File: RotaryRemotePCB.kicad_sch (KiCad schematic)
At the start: 10 parts, among them J3 i2c, J4 Neopixel Connector, J5 EncoderRotary, J6 EncoderSwitch, SW1 RotaryEncoder_Switch, U1 TP4056, U2 WeMos_D1_mini, U3 magnetic-charger, U4 TTL

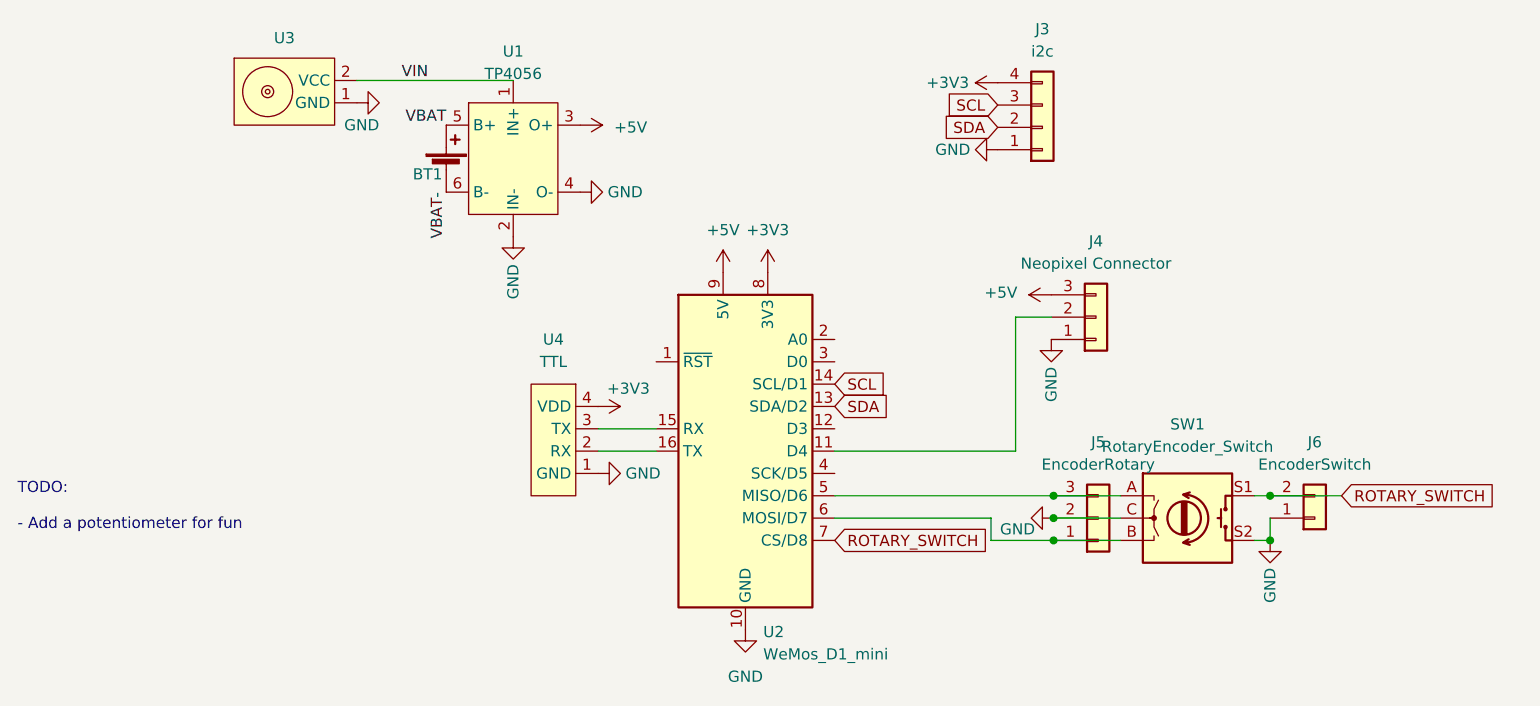
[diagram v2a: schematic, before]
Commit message: Update I2C Bus
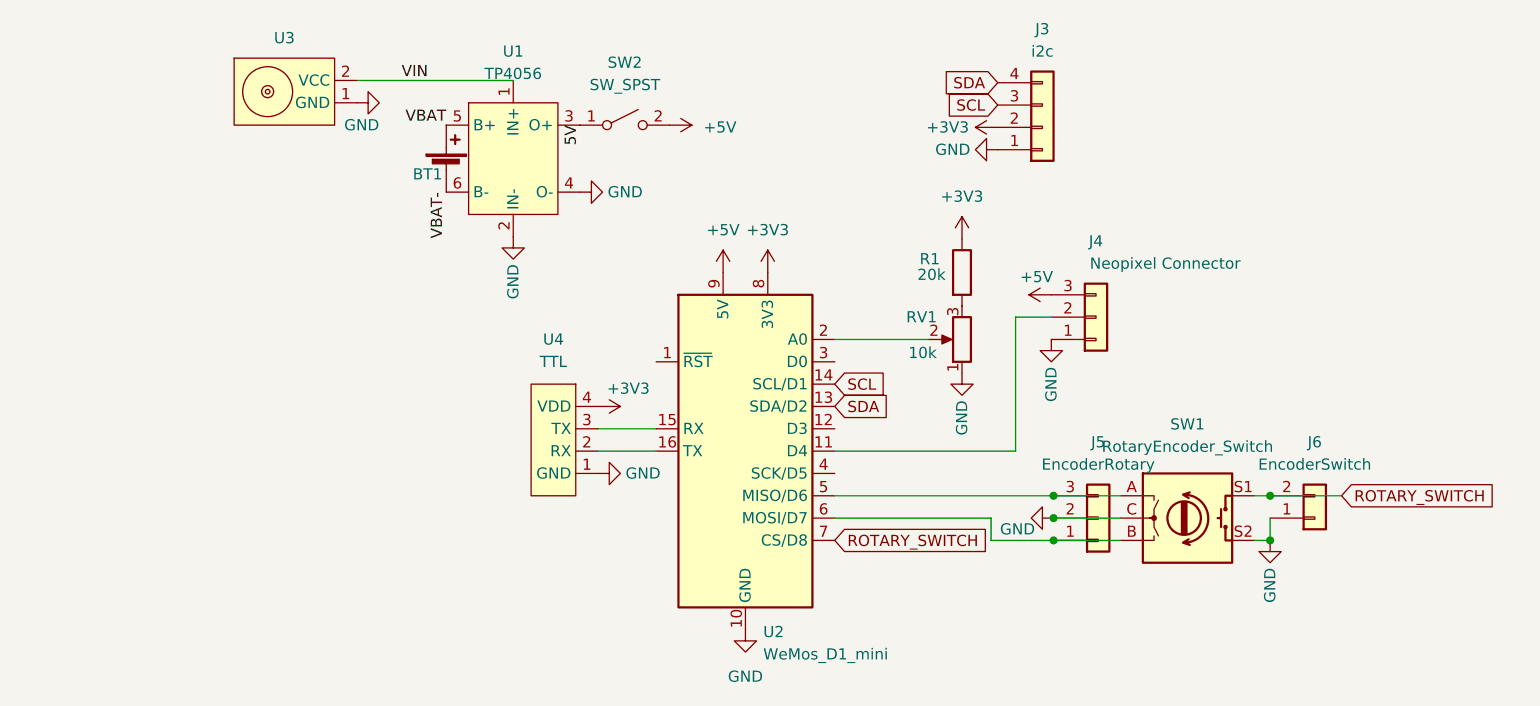
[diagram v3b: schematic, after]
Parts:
- added R1: 20k, Resistor_THT:R_Axial_DIN0207_L6.3mm_D2.5mm_P7.62mm_Horizontal, symbol Device:R
- added RV1: 10k, Potentiometer_THT:Potentiometer_Piher_PT-6-V_Vertical, symbol Device:R_Potentiometer
- added SW2: SW_SPST, Button_Switch_SMD:SW_SPDT_CK-JS102011SAQN, symbol Switch:SW_SPST
- SW1: footprint Rotary_Encoder:RotaryEncoder_Alps_EC12E-Switch_Vertical_H20mm -> (none)
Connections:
- net +3V3: now also J3.2 (Pin_2), R1.1; no longer J3.4 (Pin_4)
- net +5V: now also SW2.2 (B); no longer U1.3 (O+)
- net GND: now also RV1.1
- net SDA: now also J3.4 (Pin_4); no longer J3.2 (Pin_2)
- net at U2.2 (A0): now also RV1.2
- new net: R1.2, RV1.3
- new net 5V: SW2.1 (A), U1.3 (O+)
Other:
- note removed: "TODO: - Add a potentiometer for fun"
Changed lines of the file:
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@@
+    (stroke (width 0) (type default) (color 0 0 0 0))
+  )
+  (wire (pts (xy 181.102 68.326) (xy 191.77 68.326))
     (stroke (width 0) (type default) (color 0 0 0 0))
   )
@@
     (stroke (width 0) (type default) (color 0 0 0 0))
   )
-  (text "TODO:\n\n- Add a potentiometer for fun" (at 88.138 90.17 0)
-    (effects (font (size 1.27 1.27)) (justify left bottom))
-  )
   (label "VBAT-" (at 136.906 51.562 270)
+    (effects (font (size 1.27 1.27)) (justify right bottom))
+  )
+  (label "5V" (at 152.146 43.942 270)
     (effects (font (size 1.27 1.27)) (justify right bottom))
   )
@@
     )
   )
-  (global_label "SDA" (shape input) (at 199.644 44.196 180) (fields_autoplaced)
+  (global_label "SDA" (shape input) (at 199.644 39.116 180) (fields_autoplaced)
     (effects (font (size 1.27 1.27)) (justify right))
-    (property "Intersheet References" "${INTERSHEET_REFS}" (id 0) (at 193.6628 44.1166 0)
+    (property "Intersheet References" "${INTERSHEET_REFS}" (id 0) (at 193.6628 39.0366 0)
       (effects (font (size 1.27 1.27)) (justify right) hide)
     )
@@
       (effects (font (size 1.27 1.27)) hide)
     )
-    (property "Value" "+5V" (id 1) (at 198.12 62.992 90)
+    (property "Value" "+5V" (id 1) (at 202.184 61.214 90)
       (effects (font (size 1.27 1.27)) (justify right))
     )
@@
     (pin "4")
   )
-  (symbol (lib_id "power:+5V") (at 152.146 43.942 270) (unit 1)
-    (in_bom yes) (on_board yes)
-    (property "Reference" "#PWR0106" (id 0) (at 148.336 43.942 0)
-      (effects (font (size 1.27 1.27)) hide)
-    )
-    (property "Value" "+5V" (id 1) (at 159.766 44.196 90)
+  (symbol (lib_id "power:+5V") (at 162.306 43.942 270) (unit 1)
+    (in_bom yes) (on_board yes)
+    (property "Reference" "#PWR0106" (id 0) (at 158.496 43.942 0)
+      (effects (font (size 1.27 1.27)) hide)
+    )
+    (property "Value" "+5V" (id 1) (at 169.926 44.196 90)
       (effects (font (size 1.27 1.27)) (justify right))
     )
-    (property "Footprint" "" (id 2) (at 152.146 43.942 0)
-      (effects (font (size 1.27 1.27)) hide)
-    )
-    (property "Datasheet" "" (id 3) (at 152.146 43.942 0)
+    (property "Footprint" "" (id 2) (at 162.306 43.942 0)
+      (effects (font (size 1.27 1.27)) hide)
+    )
+    (property "Datasheet" "" (id 3) (at 162.306 43.942 0)
       (effects (font (size 1.27 1.27)) hide)
     )
@@
     (pin "4")
   )
+  (symbol (lib_id "Device:R_Potentiometer") (at 195.58 68.326 180) (unit 1)
+    (in_bom yes) (on_board yes)
+    (property "Reference" "RV1" (id 0) (at 189.23 65.786 0)
+      (effects (font (size 1.27 1.27)) (justify right))
+    )
+    (property "Value" "10k" (id 1) (at 189.484 69.85 0)
+      (effects (font (size 1.27 1.27)) (justify right))
+    )
+    (property "Footprint" "Potentiometer_THT:Potentiometer_Piher_PT-6-V_Vertical" (id 2) (at 195.58 68.326 0)
+      (effects (font (size 1.27 1.27)) hide)
+    )
+    (property "Datasheet" "~" (id 3) (at 195.58 68.326 0)
+      (effects (font (size 1.27 1.27)) hide)
+    )
+    (pin "1")
+    (pin "2")
+    (pin "3")
+  )
   (symbol (lib_id "magnetic-charger:magnetic-charger") (at 119.126 40.132 0) (unit 1)
     (in_bom yes) (on_board yes) (fields_autoplaced)
@@
     (pin "1")
   )
+  (symbol (lib_id "Switch:SW_SPST") (at 157.226 43.942 0) (unit 1)
+    (in_bom yes) (on_board yes) (fields_autoplaced)
+    (property "Reference" "SW2" (id 0) (at 157.226 36.83 0))
+    (property "Value" "SW_SPST" (id 1) (at 157.226 39.37 0))
+    (property "Footprint" "Button_Switch_SMD:SW_SPDT_CK-JS102011SAQN" (id 2) (at 157.226 43.942 0)
+      (effects (font (size 1.27 1.27)) hide)
+    )
+    (property "Datasheet" "~" (id 3) (at 157.226 43.942 0)
+      (effects (font (size 1.27 1.27)) hide)
+    )
+    (pin "1")
+    (pin "2")
+  )
+  (symbol (lib_id "power:+3V3") (at 195.58 56.896 0) (unit 1)
+    (in_bom yes) (on_board yes) (fields_autoplaced)
+    (property "Reference" "#PWR0117" (id 0) (at 195.58 60.706 0)
+      (effects (font (size 1.27 1.27)) hide)
+    )
+    (property "Value" "+3V3" (id 1) (at 195.58 52.07 0))
+    (property "Footprint" "" (id 2) (at 195.58 56.896 0)
+      (effects (font (size 1.27 1.27)) hide)
+    )
+    (property "Datasheet" "" (id 3) (at 195.58 56.896 0)
+      (effects (font (size 1.27 1.27)) hide)
+    )
+    (pin "1")
+  )
   (symbol (lib_id "Device:Battery_Cell") (at 136.906 49.022 0) (unit 1)
     (in_bom yes) (on_board yes)
@@
   )
   (symbol (lib_id "Connector_Generic:Conn_01x03") (at 210.82 65.786 0) (mirror x) (unit 1)
-    (in_bom yes) (on_board yes) (fields_autoplaced)
+    (in_bom yes) (on_board yes)
     (property "Reference" "J4" (id 0) (at 210.82 57.15 0))
-    (property "Value" "Neopixel Connector" (id 1) (at 210.82 59.69 0))
+    (property "Value" "Neopixel Connector" (id 1) (at 218.694 59.69 0))
     (property "Footprint" "Connector_PinHeader_2.54mm:PinHeader_1x03_P2.54mm_Horizontal" (id 2) (at 210.82 65.786 0)
       (effects (font (size 1.27 1.27)) hide)
@@
     (pin "2")
     (pin "3")
+  )
+  (symbol (lib_id "Device:R") (at 195.58 60.706 0) (unit 1)
+    (in_bom yes) (on_board yes)
+    (property "Reference" "R1" (id 0) (at 190.754 59.182 0)
+      (effects (font (size 1.27 1.27)) (justify left))
+    )
+    (property "Value" "20k" (id 1) (at 190.5 60.96 0)
+      (effects (font (size 1.27 1.27)) (justify left))
+    )
+    (property "Footprint" "Resistor_THT:R_Axial_DIN0207_L6.3mm_D2.5mm_P7.62mm_Horizontal" (id 2) (at 193.802 60.706 90)
+      (effects (font (size 1.27 1.27)) hide)
+    )
+    (property "Datasheet" "~" (id 3) (at 195.58 60.706 0)
+      (effects (font (size 1.27 1.27)) hide)
+    )
+    (pin "1")
+    (pin "2")
   )
   (symbol (lib_id "Connector_Generic:Conn_01x02") (at 235.712 88.646 0) (mirror x) (unit 1)
@@
     (pin "9")
   )
-  (symbol (lib_id "power:+3V3") (at 199.644 39.116 90) (unit 1)
-    (in_bom yes) (on_board yes)
-    (property "Reference" "#PWR0114" (id 0) (at 203.454 39.116 0)
-      (effects (font (size 1.27 1.27)) hide)
-    )
-    (property "Value" "+3V3" (id 1) (at 191.516 39.116 90)
+  (symbol (lib_id "power:+3V3") (at 199.644 44.196 90) (unit 1)
+    (in_bom yes) (on_board yes)
+    (property "Reference" "#PWR0114" (id 0) (at 203.454 44.196 0)
+      (effects (font (size 1.27 1.27)) hide)
+    )
+    (property "Value" "+3V3" (id 1) (at 191.516 44.196 90)
       (effects (font (size 1.27 1.27)) (justify right))
     )
-    (property "Footprint" "" (id 2) (at 199.644 39.116 0)
-      (effects (font (size 1.27 1.27)) hide)
-    )
-    (property "Datasheet" "" (id 3) (at 199.644 39.116 0)
+    (property "Footprint" "" (id 2) (at 199.644 44.196 0)
+      (effects (font (size 1.27 1.27)) hide)
+    )
+    (property "Datasheet" "" (id 3) (at 199.644 44.196 0)
       (effects (font (size 1.27 1.27)) hide)
     )
@@
     (property "Reference" "SW1" (id 0) (at 221.234 77.978 0))
     (property "Value" "RotaryEncoder_Switch" (id 1) (at 221.234 80.518 0))
-    (property "Footprint" "Rotary_Encoder:RotaryEncoder_Alps_EC12E-Switch_Vertical_H20mm" (id 2) (at 217.424 84.582 0)
+    (property "Footprint" "" (id 2) (at 217.424 84.582 0)
       (effects (font (size 1.27 1.27)) hide)
     )
@@
     (pin "S2")
   )
+  (symbol (lib_id "power:GND") (at 195.58 72.136 0) (unit 1)
+    (in_bom yes) (on_board yes)
+    (property "Reference" "#PWR0116" (id 0) (at 195.58 78.486 0)
+      (effects (font (size 1.27 1.27)) hide)
+    )
+    (property "Value" "GND" (id 1) (at 195.58 79.248 90)
+      (effects (font (size 1.27 1.27)) (justify left))
+    )
+    (property "Footprint" "" (id 2) (at 195.58 72.136 0)
+      (effects (font (size 1.27 1.27)) hide)
+    )
+    (property "Datasheet" "" (id 3) (at 195.58 72.136 0)
+      (effects (font (size 1.27 1.27)) hide)
+    )
+    (pin "1")
+  )
   (symbol (lib_id "Connector_Generic:Conn_01x03") (at 211.074 88.646 0) (mirror x) (unit 1)
     (in_bom yes) (on_board yes) (fields_autoplaced)
@@
       (reference "#PWR0115") (unit 1) (value "GND") (footprint "")
     )
+    (path "/c6b6654f-d4d6-433c-9ddf-8dffc929a737"
+      (reference "#PWR0116") (unit 1) (value "GND") (footprint "")
+    )
+    (path "/75c0d22b-b588-46e1-b175-3a3914ab870b"
+      (reference "#PWR0117") (unit 1) (value "+3V3") (footprint "")
+    )
     (path "/764ea05b-a7e6-4125-9b56-e599a75fd2e3"
       (reference "BT1") (unit 1) (value "Battery_Cell") (footprint "Connector_JST:JST_EH_S2B-EH_1x02_P2.50mm_Horizontal")
@@
       (reference "J6") (unit 1) (value "EncoderSwitch") (footprint "Connector_PinHeader_2.54mm:PinHeader_1x02_P2.54mm_Vertical")
     )
+    (path "/930bff3d-a2da-4770-9119-e0511b5dafd8"
+      (reference "R1") (unit 1) (value "20k") (footprint "Resistor_THT:R_Axial_DIN0207_L6.3mm_D2.5mm_P7.62mm_Horizontal")
+    )
+    (path "/454653bd-ad50-4b62-92ea-c0c57c8f882a"
+      (reference "RV1") (unit 1) (value "10k") (footprint "Potentiometer_THT:Potentiometer_Piher_PT-6-V_Vertical")
+    )
     (path "/c1717db9-c59d-4db0-b83d-cde4fd1a09fb"
-      (reference "SW1") (unit 1) (value "RotaryEncoder_Switch") (footprint "Rotary_Encoder:RotaryEncoder_Alps_EC12E-Switch_Vertical_H20mm")
+      (reference "SW1") (unit 1) (value "RotaryEncoder_Switch") (footprint "")
+    )
+    (path "/5b44afe4-972a-4b92-a34d-bd0b1864de75"
+      (reference "SW2") (unit 1) (value "SW_SPST") (footprint "Button_Switch_SMD:SW_SPDT_CK-JS102011SAQN")
     )
     (path "/e828b3d1-2829-4116-a8ae-3983b1907dc2"
